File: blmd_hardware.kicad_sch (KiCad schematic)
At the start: 88 parts, among them J1 MR30PW-F, J2 control, J3 GND, J4 12V, J5 STLink/V2, J6 STLink-V3, Q1 RH6L040BG, Q2 RH6L040BG, Q3 RH6L040BG, Q4 RH6L040BG, Q5 RH6L040BG, Q6 RH6L040BG, SW1 reset, SW2 SW_DIP_x04, U1 LM5106MMX_NOPB, U10 STM32F303K8T6, U2 LM5106MMX_NOPB, U3 LM5106MMX_NOPB, U4 SI8620BB-B-IS, U5 SI8620BB-B-IS, U6 ACS72981LLRATR-050B3, U7 ACS72981LLRATR-050B3, U8 AP7375(SA), U9 BD41041FJ-C

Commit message: temporary place parts
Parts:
- removed R10, R11, R12, R13, R14, R21, R27, R9: 10k, Resistor_SMD:R_0603_1608Metric_Pad0.98x0.95mm_HandSolder, symbol Device:R
- SW2: value SW_DIP_x04 -> KHS42E
- renumbered R16 to R10, R17 to R11, R18 to R12, R19 to R13, R20 to R14, R22 to R15, R23 to R16, R24 to R17, R25 to R18, R26 to R19, R28 to R20, R29 to R21, R30 to R22, R15 to R9
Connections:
- net GNDD: now also U5.3 (VIB)
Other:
- moved on the sheet: R3, R4, R5, R6, R7, R8

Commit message: complete
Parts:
- removed C14: 0.1u, Capacitor_SMD:C_0603_1608Metric_Pad1.08x0.95mm_HandSolder, symbol Device:C
- removed C20: 1u, Capacitor_SMD:C_0603_1608Metric_Pad1.08x0.95mm_HandSolder, symbol Device:C
- removed U10: STM32F303K8T6, Package_QFP:LQFP-32_7x7mm_P0.8mm, symbol MCU_ST_STM32F3:STM32F303K8Tx
- removed U8: AP7375(SA), Package_TO_SOT_SMD:SOT-23-3, symbol blmd:AP7375(SA)
- added U10: STM32G431KBTx, Package_QFP:LQFP-32_7x7mm_P0.8mm, symbol MCU_ST_STM32G4:STM32G431KBTx
- added U8: BD950N1G-C, Package_SO:TSOP-5_1.65x3.05mm_P0.95mm, symbol blmd:BD950N1G-C
- C19: renamed from C21; value 1u -> 0.047u
- C20: renamed from C22; value 10u -> 0.1u
- renumbered C15 to C14, C16 to C15, C17 to C16, C18 to C17, C19 to C18, C23 to C21, C24 to C22, R31 to R23, R32 to R24
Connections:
- net +12V: now also U8.4 (VIN)
- net +3V3: now also U10.1 (VDD), U10.15 (VDDA), U10.17 (VDD)
- net +5V: now also U8.5 (VOUT)
- net GND: now also U8.2 (GND)
- net GNDD: now also U10.14 (VSSA), U10.16 (VSS), U10.32 (VSS)
- net ID1: now also U10.9 (PA4)
- net ID2: now also U10.10 (PA5)
- net ID3: now also U10.18 (PA8)
- net ID4: now also U10.19 (PA9)
- net ID_DISP: now also U10.27 (PB4)
- net NRST: now also U10.4 (PG10)
- net RXD: now also U10.21 (PA11)
- net SCA: now also U10.5 (PA0)
- net SCC: now also U10.6 (PA1)
- net SIGA: now also U10.11 (PA6)
- net SIGB: now also U10.12 (PA7)
- net SIGC: now also U10.13 (PB0)
- net SPD1: now also U10.29 (PB6)
- net SPD2: now also U10.30 (PB7)
- net STATUS: now also U10.28 (PB5)
- net SWCLK: now also U10.24 (PA14)
- net SWDIO: now also U10.23 (PA13)
- net SWO: now also U10.26 (PB3)
- net TXD: now also U10.22 (PA12)
- net USART_RX: now also U10.8 (PA3)
- net USART_TX: now also U10.7 (PA2)
- net at R19.1: now also U10.31 (PB8)
- no-connect marks 17 -> 16
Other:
- moved on the sheet: C12, C13, C21, R19, SW1

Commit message: repaterning...
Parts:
- removed J5: STLink/V2, Connector_PinSocket_2.54mm:PinSocket_1x06_P2.54mm_Horizontal, symbol Connector:Conn_01x06_Socket
- removed U6, U7: ACS72981LLRATR-050B3, Sensor_Current:Allegro_PSOF-7_4.8x6.4mm_P1.60mm, symbol Sensor_Current:ACS781xLRTR-150U
- added U6, U7: ACS711KEXLT-31AB, Sensor_Current:Allegro_QFN-12-10-1EP_3x3mm_P0.5mm, symbol Sensor_Current:ACS711xEXLT-31AB
- R20: renamed from R23; value 100 -> 10k
- R21: renamed from R24; value 100 -> 10k
- renumbered J6 to J5, R20 to R22, R21 to R23, R22 to R24
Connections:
- net +3V3: now also R20.1, R21.2, U6.10 (VCC), U7.10 (VCC)
- net GNDD: now also U6.3 (GND), U7.3 (GND)
- net HSA: now also U6.1 (IP+)
- net HSC: now also U7.2 (IP-)
- net SCA: now also U6.9 (VIOUT); no longer R20.1
- net SCC: now also U7.9 (VIOUT); no longer R21.1
- net SOA: now also U6.2 (IP-)
- net SOC: now also U7.1 (IP+)
- net at R20.2: now also U6.4 (~{FAULT})
- new net: R21.1, U7.4 (~{FAULT})
- no-connect marks 16 -> 19
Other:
- moved on the sheet: C13, C15, C16, C17, C18, C19, C20, C21, C22, D5, D7, D8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

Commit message: back up commit
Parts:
- removed C11, C20, C9: 0.1u, Capacitor_SMD:C_0603_1608Metric_Pad1.08x0.95mm_HandSolder, symbol Device:C
- removed C19: 0.047u, Capacitor_SMD:C_0603_1608Metric_Pad1.08x0.95mm_HandSolder, symbol Device:C
- removed D2, D3, D4: D, Diode_SMD:D_SOD-323F, symbol Device:D
- removed D5: D_Schottky, Diode_SMD:D_SOD-523, symbol Device:D_Schottky
- removed R1, R2: 0, Resistor_SMD:R_0603_1608Metric_Pad0.98x0.95mm_HandSolder, symbol Device:R
- removed R10, R11, R13, R14, R15, R16, R17, R18, R9: 10k, Resistor_SMD:R_0603_1608Metric_Pad0.98x0.95mm_HandSolder, symbol Device:R
- removed U1, U2, U3: LM5106MMX_NOPB, Package_SO:TSSOP-10_3x3mm_P0.5mm, symbol blmd:LM5106MMX_NOPB
- removed U4, U5: SI8620BB-B-IS, Package_SO:SOIC-8_3.9x4.9mm_P1.27mm, symbol Isolator:ADuM120N
- removed U8: BD950N1G-C, Package_SO:TSOP-5_1.65x3.05mm_P0.95mm, symbol blmd:BD950N1G-C
- added C7: 0.22u, Capacitor_SMD:C_0603_1608Metric_Pad1.08x0.95mm_HandSolder, symbol Device:C
- added D2: blue, LED_SMD:LED_0603_1608Metric_Pad1.05x0.95mm_HandSolder, symbol Device:LED
- added R7: 15k, Resistor_SMD:R_0603_1608Metric_Pad0.98x0.95mm_HandSolder, symbol Device:R
- added R8: 10k, Resistor_SMD:R_0603_1608Metric_Pad0.98x0.95mm_HandSolder, symbol Device:R
- added U1: A4939KLPTR-5-T, Package_SO:HTSSOP-28-1EP_4.4x9.7mm_P0.65mm_EP2.75x6.2mm, symbol blmd:A4939KLPTR-5-T
- added U4: ISO7760FDBQR, Package_SO:SSOP-16_3.9x4.9mm_P0.635mm, symbol Isolator:Si8660BA-AS1
- C6: value 0.47u -> 1u
- C8: renamed from C5; value 0.47u -> 10u
- R12: value 10k -> 2.2k
- renumbered C22 to C10, C13 to C11, C10 to C12, C8 to C13, C15 to C14, C16 to C15, C17 to C16, C18 to C17, C12 to C18, C14 to C19, C4 to C3, C3 to C4, C7 to C5, C21 to C9, D6 to D3, D7 to D4, D8 to D5, R3 to R1, R20 to R10, R19 to R11, R22 to R13, R23 to R14, R24 to R15, R6 to R2, R4 to R3, R7 to R4, R8 to R6, R21 to R9
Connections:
- net +12VA: now also C7.1, U1.17 (VBB), U1.18 (VBRG)
- net +3V3: now also U4.1 (VDD1)
- net +5V: now also C6.1, R12.2, R7.2, U1.20 (V5), U4.16 (VDD2)
- net GNDD: now also U4.8 (GND1); no longer R12.2
- net GNDPWR: now also C13.2, C6.2, C8.1, D3.1 (K), C7.2, R8.2, U1.1 (LSS), U1.19 (GND), U1.29 (PAD), U4.9 (GND2)
- net HOA: now also U1.11 (GHA)
- net HOB: now also U1.7 (GHB)
- net HOC: now also U1.3 (GHC)
- net HSA: now also U1.12 (SA)
- net HSB: now also C3.1, U1.8 (SB); no longer C4.1
- net HSC: now also C4.1, U1.4 (SC); no longer C3.1
- net ID3: now also U10.11 (PA6); no longer U10.18 (PA8)
- net ID4: now also U10.25 (PA15); no longer U10.19 (PA9)
- net ID_DISP: now also U10.30 (PB7); no longer U10.27 (PB4)
- net LOA: now also U1.10 (GLA)
- net LOB: now also U1.6 (GLB)
- net LOC: now also U1.2 (GLC)
- net PWMA: now also U1.23 (AHI), U4.15 (B1)
- net PWMB: now also U1.25 (BHI), U4.13 (B3)
- net PWMC: now also U1.27 (CHI), U4.11 (B5)
- net SIGA: now also U10.18 (PA8), U4.2 (A1); no longer R12.1, U10.11 (PA6)
- net SIGB: now also U10.19 (PA9), U4.4 (A3); no longer U10.12 (PA7)
- net SIGC: now also U10.20 (PA10), U4.6 (A5); no longer U10.13 (PB0)
- net SPD1: now also J2.3 (Pin_3), U10.27 (PB4); no longer J2.5 (Pin_5), U10.29 (PB6)
- net SPD2: now also J2.5 (Pin_5), U10.28 (PB5); no longer J2.3 (Pin_3), U10.30 (PB7)
- net STATUS: now also U10.29 (PB6); no longer U10.28 (PB5)
- net SIGC_N: now reaches U10.2 (PF0)
- net SIGC_N: now also U4.7 (A6)
- net at C3.2: now also U1.9 (CB)
- net at C4.2: now also U1.5 (CC)
- net at C2.2: now also U1.13 (CA)
- removed net +12V: C5.1, C6.1, C8.1
- removed net GND: C13.2, C5.2, C6.2, C8.2, D3.1 (K)
- new net: C8.2, U1.14 (VREG)
- new net: C5.2, U1.15 (CP2)
- new net: C5.1, U1.16 (CP1)
- new net: R7.1, R8.1, U1.21 (VDSTH)
- new net: D2.1 (K), U1.22 (FAULT)
- new net: D2.2 (A), R12.1
- new net PWMA_N: U1.24 (ALO), U4.14 (B2)
- new net PWMB_N: U1.26 (BLO), U4.12 (B4)
- new net PWMC_N: U1.28 (CLO), U4.10 (B6)
- new net SIGA_N: U10.12 (PA7), U4.3 (A2)
- new net SIGB_N: U10.13 (PB0), U4.5 (A4)
- no-connect marks 19 -> 15
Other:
- moved on the sheet: C12, C13, C2, C3, C4, C5, C8, SW2

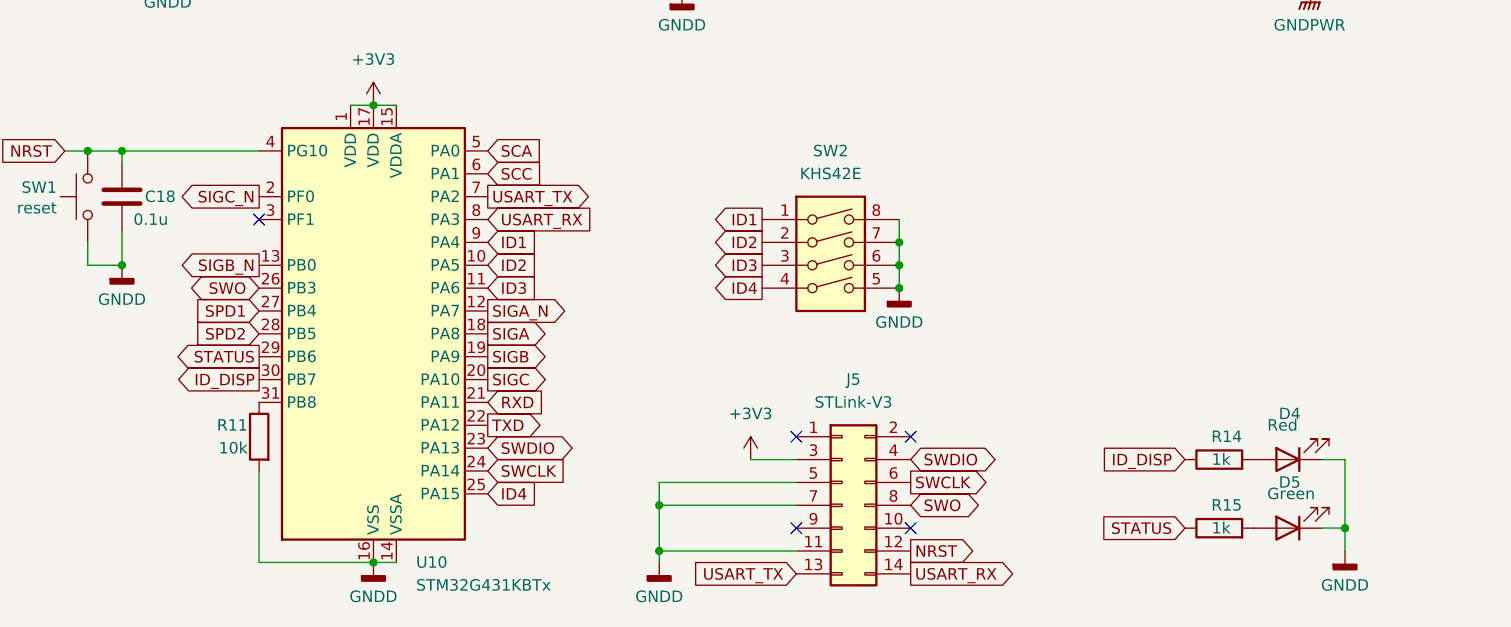
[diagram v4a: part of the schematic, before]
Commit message: fix : vdd vss position
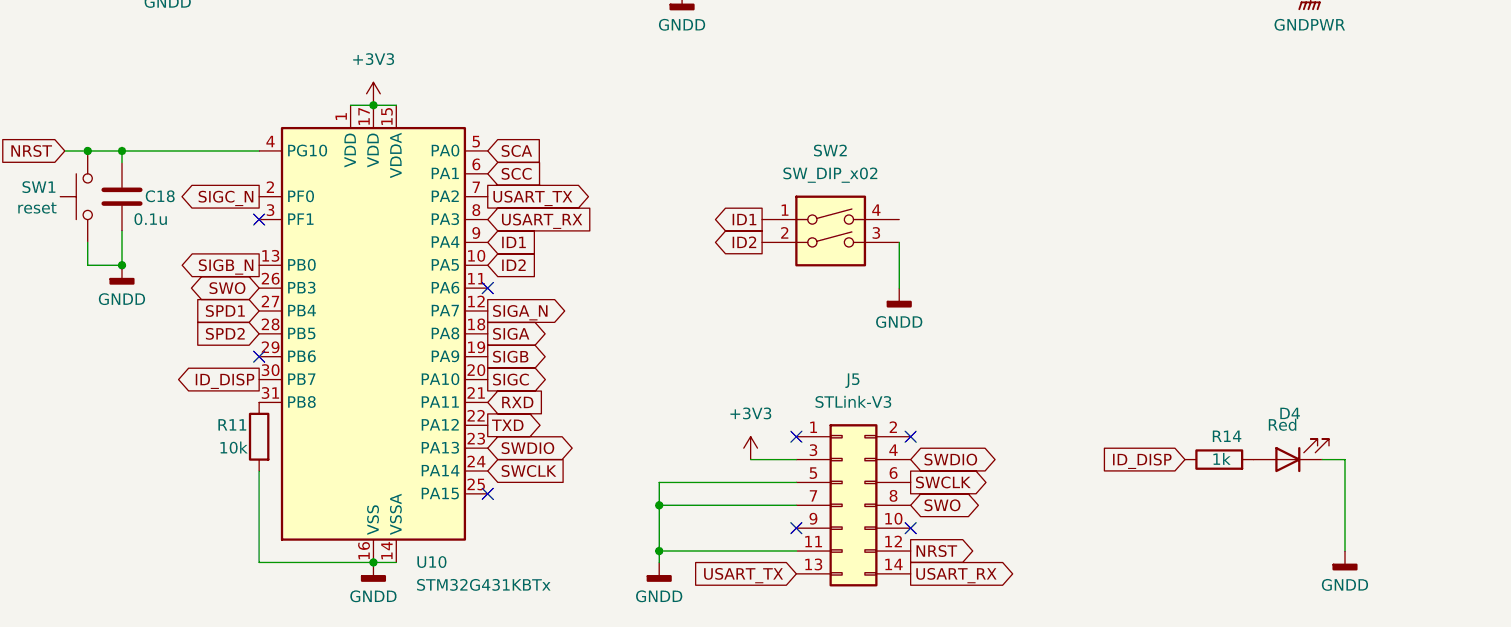
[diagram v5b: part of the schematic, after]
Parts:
- removed D5: Green, LED_SMD:LED_0603_1608Metric_Pad1.05x0.95mm_HandSolder, symbol Device:LED
- removed R15: 1k, Resistor_SMD:R_0603_1608Metric_Pad0.98x0.95mm_HandSolder, symbol Device:R
- removed SW2: KHS42E, Button_Switch_SMD:SW_DIP_SPSTx04_Slide_Copal_CHS-04B_W7.62mm_P1.27mm, symbol Switch:SW_DIP_x04
- added SW2: SW_DIP_x02, Button_Switch_SMD:SW_DIP_SPSTx02_Slide_Copal_CHS-02B_W7.62mm_P1.27mm, symbol Switch:SW_DIP_x02
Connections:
- net GNDD: now also SW2.3
- net ID1: now also SW2.1
- net ID2: now also SW2.2
- net ID3: no longer names the net of U10.11 (PA6)
- net ID4: no longer names the net of U10.25 (PA15)
- net STATUS: no longer names the net of U10.29 (PB6)
- no-connect marks 15 -> 18

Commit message: backup commit
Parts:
- removed C13: 0.1u, Capacitor_SMD:C_0603_1608Metric_Pad1.08x0.95mm_HandSolder, symbol Device:C
- renumbered C19 to C13
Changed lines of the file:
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@@
 	)
 	(junction
-		(at 255.27 128.27)
-		(diameter 0)
-		(color 0 0 0 0)
-	)
-	(junction
 		(at 38.1 77.47)
 		(diameter 0)
@@
 	)
 	(junction
-		(at 255.27 151.13)
-		(diameter 0)
-		(color 0 0 0 0)
-	)
-	(junction
 		(at 38.1 100.33)
 		(diameter 0)
@@
 	(wire
 		(pts
-			(xy 242.57 128.27) (xy 255.27 128.27)
-		)
-		(stroke
-			(width 0)
-			(type default)
-		)
-	)
-	(wire
-		(pts
 			(xy 168.91 175.26) (xy 168.91 185.42)
 		)
@@
 	(wire
 		(pts
-			(xy 255.27 151.13) (xy 255.27 152.4)
-		)
-		(stroke
-			(width 0)
-			(type default)
-		)
-	)
-	(wire
-		(pts
 			(xy 38.1 120.65) (xy 50.8 120.65)
 		)
@@
 	(wire
 		(pts
-			(xy 255.27 142.24) (xy 255.27 151.13)
-		)
-		(stroke
-			(width 0)
-			(type default)
-		)
-	)
-	(wire
-		(pts
 			(xy 92.71 180.34) (xy 107.95 180.34)
 		)
@@
 	(wire
 		(pts
-			(xy 242.57 151.13) (xy 255.27 151.13)
+			(xy 242.57 151.13) (xy 243.84 151.13)
 		)
 		(stroke
@@
 	(wire
 		(pts
-			(xy 255.27 127) (xy 255.27 128.27)
+			(xy 242.57 128.27) (xy 243.84 128.27)
 		)
 		(stroke
@@
 	(wire
 		(pts
-			(xy 255.27 128.27) (xy 255.27 134.62)
-		)
-		(stroke
-			(width 0)
-			(type default)
-		)
-	)
-	(wire
-		(pts
 			(xy 25.4 80.01) (xy 25.4 77.47)
 		)
@@
 		(on_board yes)
 		(dnp no)
-		(property "Reference" "C19"
+		(property "Reference" "C13"
 			(at 25.4 109.22 0)
 			(effects
@@
 			(project ""
 				(path "/37d90e90-2887-4e3b-9cff-6b0fbe1d33ab"
-					(reference "C19")
+					(reference "C13")
 					(unit 1)
 				)
@@
 	(symbol
 		(lib_id "power:GNDPWR")
-		(at 255.27 152.4 0)
+		(at 243.84 151.13 0)
 		(unit 1)
 		(exclude_from_sim no)
@@
 		(fields_autoplaced yes)
 		(property "Reference" "#PWR03"
-			(at 255.27 157.48 0)
+			(at 243.84 156.21 0)
 			(effects
 				(font
@@
 		)
 		(property "Value" "GNDPWR"
-			(at 255.143 156.21 0)
+			(at 243.713 154.94 0)
 			(effects
 				(font
@@
 		)
 		(property "Footprint" ""
-			(at 255.27 153.67 0)
+			(at 243.84 152.4 0)
 			(effects
 				(font
@@
 		)
 		(property "Datasheet" ""
-			(at 255.27 153.67 0)
+			(at 243.84 152.4 0)
 			(effects
 				(font
@@
 		)
 		(property "Description" "Power symbol creates a global label with name \"GNDPWR\" , global ground"
-			(at 255.27 152.4 0)
+			(at 243.84 151.13 0)
 			(effects
 				(font
@@
 	)
 	(symbol
-		(lib_id "Device:C")
-		(at 255.27 138.43 0)
-		(unit 1)
-		(exclude_from_sim no)
-		(in_bom yes)
-		(on_board yes)
-		(dnp no)
-		(fields_autoplaced yes)
-		(property "Reference" "C13"
-			(at 259.08 137.1599 0)
-			(effects
-				(font
-					(size 1.27 1.27)
-				)
-				(justify left)
-			)
-		)
-		(property "Value" "0.1u"
-			(at 259.08 139.6999 0)
-			(effects
-				(font
-					(size 1.27 1.27)
-				)
-				(justify left)
-			)
-		)
-		(property "Footprint" "Capacitor_SMD:C_0603_1608Metric_Pad1.08x0.95mm_HandSolder"
-			(at 256.2352 142.24 0)
-			(effects
-				(font
-					(size 1.27 1.27)
-				)
-				(hide yes)
-			)
-		)
-		(property "Datasheet" "~"
-			(at 255.27 138.43 0)
-			(effects
-				(font
-					(size 1.27 1.27)
-				)
-				(hide yes)
-			)
-		)
-		(property "Description" "Unpolarized capacitor"
-			(at 255.27 138.43 0)
-			(effects
-				(font
-					(size 1.27 1.27)
-				)
-				(hide yes)
-			)
-		)
-		(pin "1"
-		)
-		(pin "2"
-		)
-		(instances
-			(project ""
-				(path "/37d90e90-2887-4e3b-9cff-6b0fbe1d33ab"
-					(reference "C13")
-					(unit 1)
-				)
-			)
-		)
-	)
-	(symbol
 		(lib_id "power:GNDD")
 		(at 247.65 62.23 0)
@@
 	(symbol
 		(lib_id "power:+5V")
-		(at 255.27 127 0)
+		(at 243.84 128.27 0)
+		(mirror y)
 		(unit 1)
 		(exclude_from_sim no)
@@
 		(on_board yes)
 		(dnp no)
-		(fields_autoplaced yes)
 		(property "Reference" "#PWR026"
-			(at 255.27 130.81 0)
+			(at 243.84 132.08 0)
 			(effects
 				(font
@@
 		)
 		(property "Value" "+5V"
-			(at 255.27 121.92 0)
+			(at 243.84 123.19 0)
 			(effects
 				(font
@@
 		)
 		(property "Footprint" ""
-			(at 255.27 127 0)
+			(at 243.84 128.27 0)
 			(effects
 				(font
@@
 		)
 		(property "Datasheet" ""
-			(at 255.27 127 0)
+			(at 243.84 128.27 0)
 			(effects
 				(font
@@
 		)
 		(property "Description" "Power symbol creates a global label with name \"+5V\""
-			(at 255.27 127 0)
+			(at 243.84 128.27 0)
 			(effects
 				(font

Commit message: tmp : complete?
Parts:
- added R15, R16: 3.3k, Resistor_SMD:R_0603_1608Metric_Pad0.98x0.95mm_HandSolder, symbol Device:R
- C16, C17: value 0.1u -> 0.01u
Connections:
- net GNDD: now also SW2.4
- net SCA: now also U10.6 (PA1), R15.1; no longer U10.5 (PA0), U6.9 (VIOUT)
- net SCC: now also U10.8 (PA3), R16.1; no longer U10.6 (PA1), U7.9 (VIOUT)
- net USART_RX: no longer names the net of J5.14 (Pin_14)
- net USART_RX: no longer U10.8 (PA3)
- net USART_TX: no longer names the net of U10.7 (PA2)
- net USART_TX: no longer J5.13 (Pin_13)
- new net: R16.2, U7.9 (VIOUT)
- new net: R15.2, U6.9 (VIOUT)
- no-connect marks 18 -> 22
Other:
- moved on the sheet: C1, C10, C11, C12, C14, C15, C16, C17, C2, C3, C4, C5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

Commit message: backup commit
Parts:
- removed R11: 10k, Resistor_SMD:R_0603_1608Metric_Pad0.98x0.95mm_HandSolder, symbol Device:R
- added C16: 0.1u, Capacitor_SMD:C_0603_1608Metric_Pad1.08x0.95mm_HandSolder, symbol Device:C
- added R16, R17, R18, R19, R20, R21: 33k, Resistor_SMD:R_0603_1608Metric_Pad0.98x0.95mm_HandSolder, symbol Device:R
- Q1, Q2, Q3, Q4, Q5, Q6: value RH6L040BG -> RH6G040CH
- R1, R2, R3, R4, R5, R6: value 39 -> 15
- renumbered C18 to C17, C16 to C18, C17 to C19, R9 to R10, R12 to R11, R13 to R12, R14 to R13, R15 to R14, R16 to R15, R10 to R9
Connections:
- net +5V: now also C16.1
- net GNDPWR: now also C16.2
- net HSA: now also R16.2, R19.2
- net HSB: now also R17.2, R20.2
- net HSC: now also R18.2, R21.2
- net ID1: now also SW2.2, U10.30 (PB7); no longer SW2.1, U10.9 (PA4)
- net ID2: now also SW2.1, U10.25 (PA15); no longer SW2.2, U10.10 (PA5)
- net ID_DISP: now also U10.19 (PA9); no longer U10.30 (PB7)
- net RXD: now also U10.31 (PB8); no longer U10.21 (PA11)
- net SCA: now also U10.8 (PA3); no longer U10.6 (PA1)
- net SCC: now also U10.13 (PB0); no longer U10.8 (PA3)
- net SIGA_N: now also U10.21 (PA11); no longer U10.12 (PA7)
- net SIGB: now also U10.11 (PA6); no longer U10.19 (PA9)
- net SIGB_N: now also U10.29 (PB6); no longer U10.13 (PB0)
- net REF0: now reaches U10.3 (PF1)
- net REF0: now also U10.7 (PA2), U10.9 (PA4), R19.1, R20.1, R21.1
- net at U10.5 (PA0): now also R18.1
- new net: R17.1, U10.12 (PA7)
- new net: R16.1, U10.6 (PA1)
- no-connect marks 22 -> 17
